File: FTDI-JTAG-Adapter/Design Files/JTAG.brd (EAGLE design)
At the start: 50 x 29 mm, 10 parts

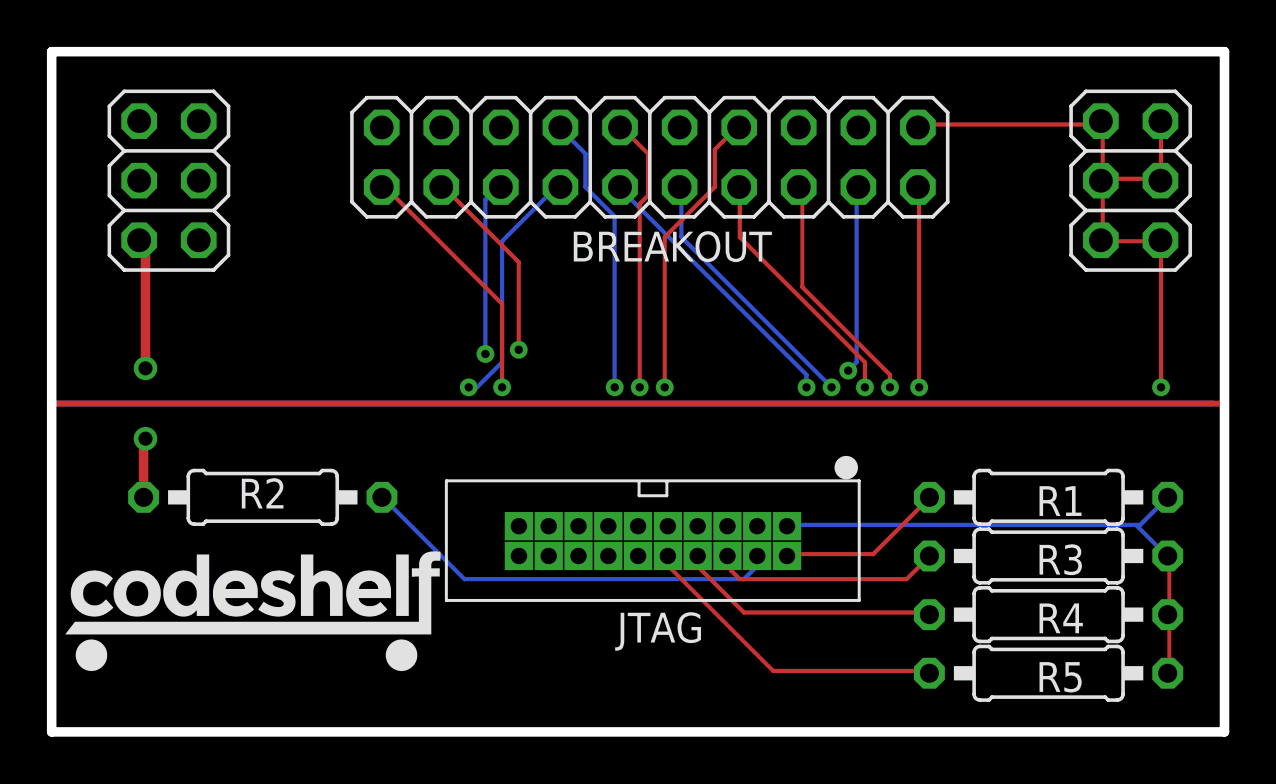
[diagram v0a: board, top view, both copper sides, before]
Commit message: Redo the JTAG mini header to be SMD
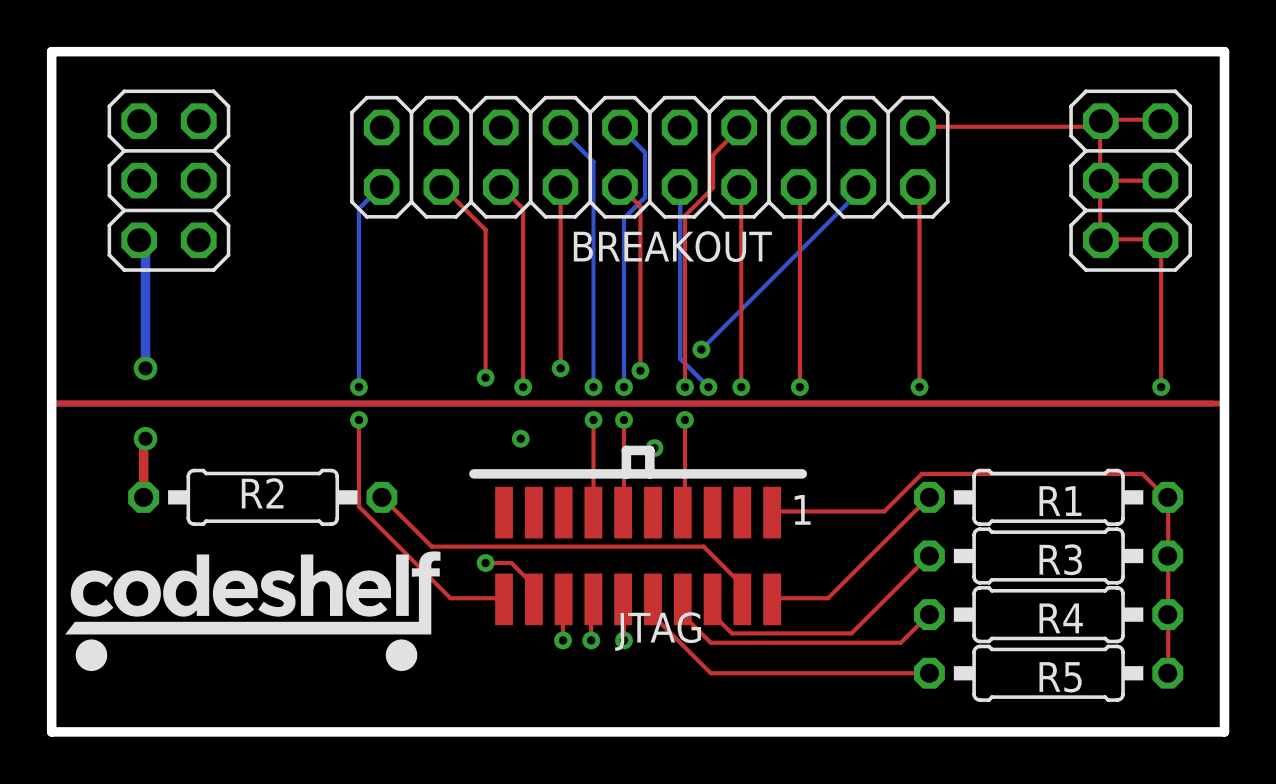
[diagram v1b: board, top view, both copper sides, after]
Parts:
- JTAG: value (none) -> 2X10JTAGSMD; device KW2:2X10JTAG -> KW2:2X10JTAG-SMD
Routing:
- net N$7: track 27.5 -> 21.8 mm, vias 1 -> 2
- net N$3: track 38.1 -> 43.6 mm
- net N$11: track 18.5 -> 21.9 mm, vias 1 -> 2
- net N$8: track 24.6 -> 21.7 mm, vias 1 -> 2
- net N$14: track 19.8 -> 17.4 mm, vias 1 -> 2
- net 3V3: track 55.6 -> 57.5 mm
- net N$4: track 27.9 -> 29.6 mm
- net N$27: track 18.5 -> 17.0 mm, vias 1 -> 2
- net N$10: track 21.3 -> 19.9 mm, vias 1 -> 2
- net N$2: track 20.6 -> 22.0 mm
- net N$9: track 20.8 -> 22.2 mm, vias 1 -> 2
- net N$5: track 32.8 -> 33.8 mm
- net N$16: track 17.7 -> 17.2 mm, vias 1 -> 2
- net GND: track 11.4 -> 11.3 mm, vias 2 -> 4
